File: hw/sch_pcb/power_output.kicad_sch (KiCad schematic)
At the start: 3 parts, among them J2 CONN1_1, J3 CONN1_1, J4 JUMP_4X2

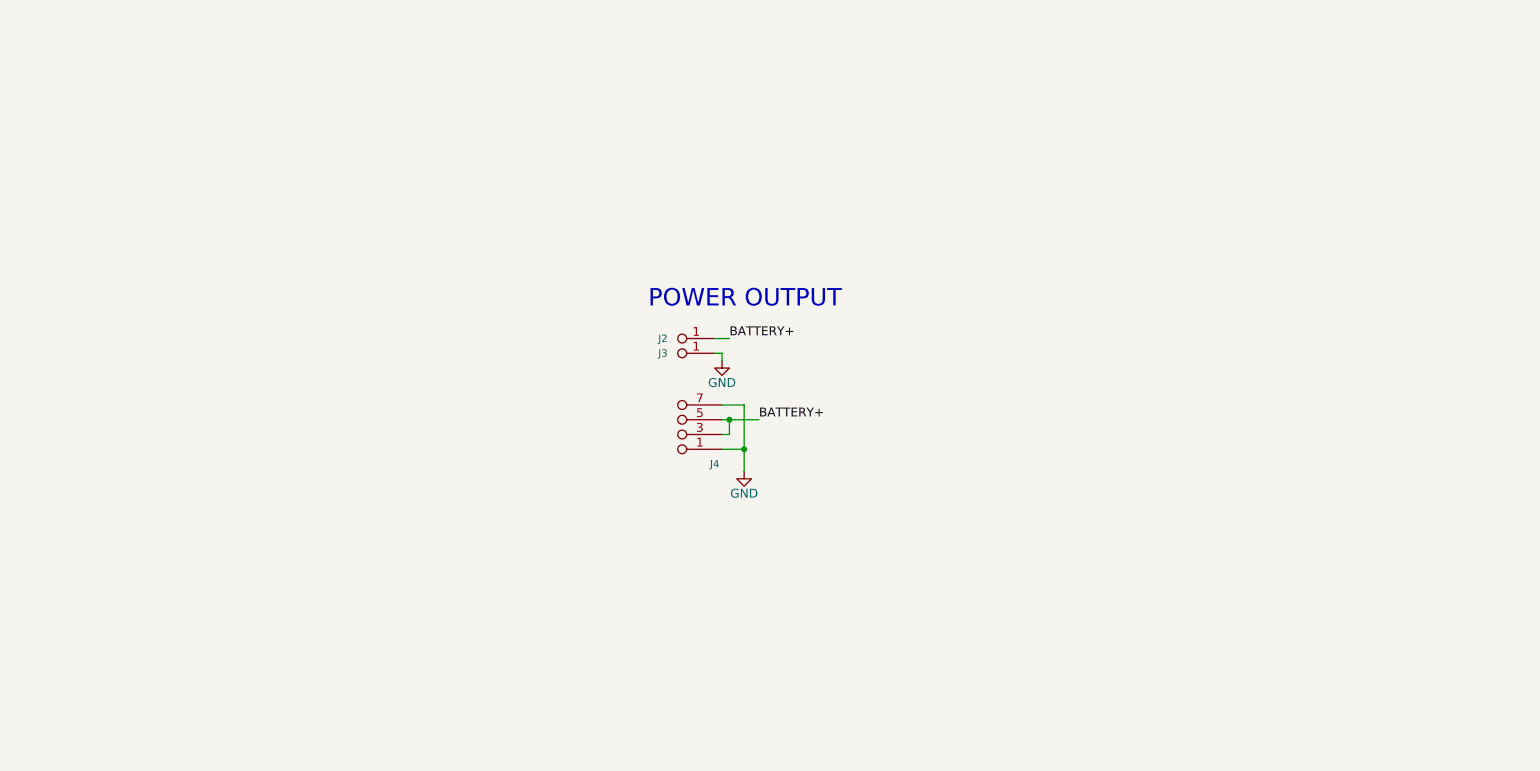
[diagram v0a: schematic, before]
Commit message: Schematics work. PCB layout initial schematics import.
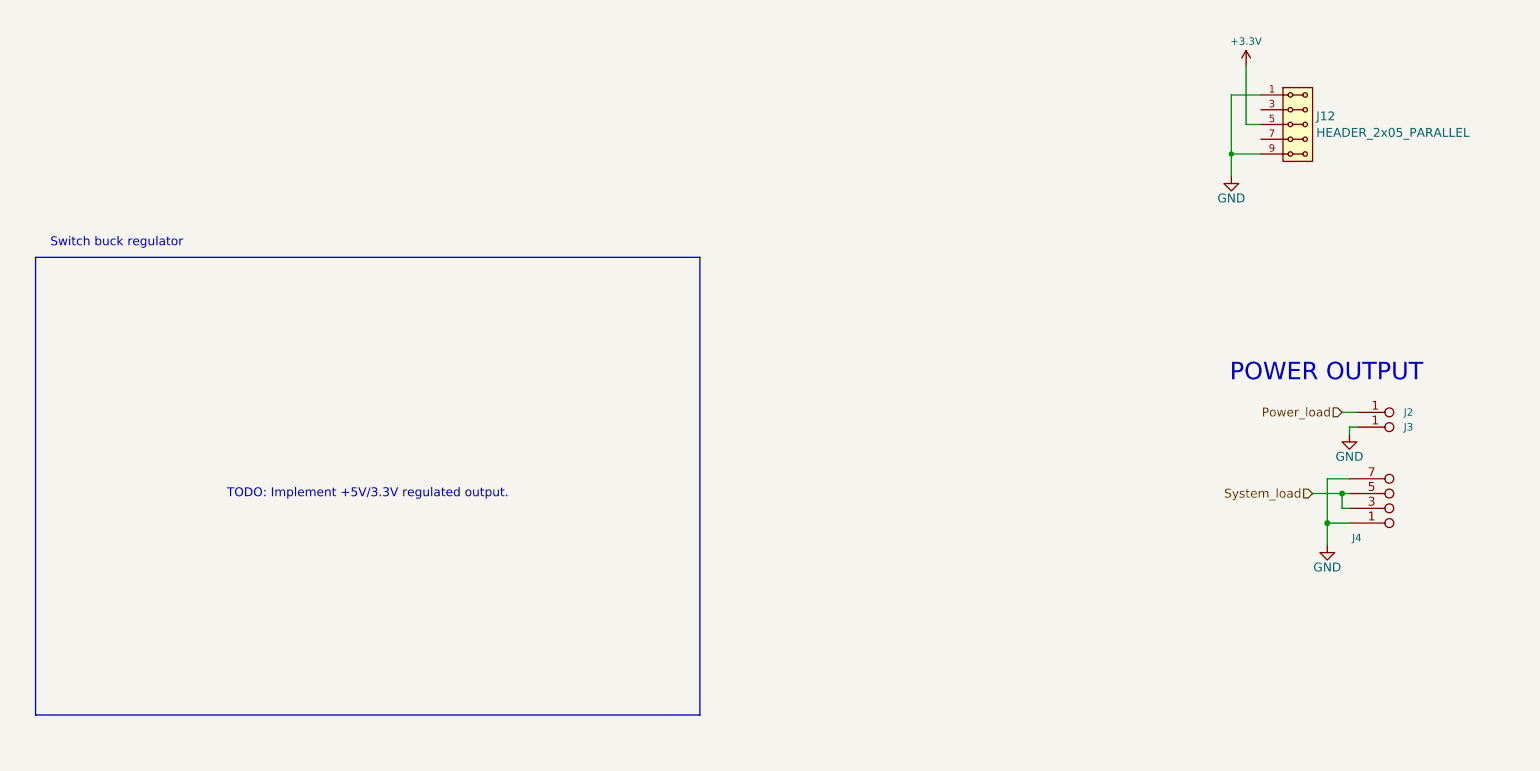
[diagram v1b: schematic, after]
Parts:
- added J12: HEADER_2x05_PARALLEL, Mlab_Pin_Headers:Straight_2x05, symbol MLAB_HEADER:HEADER_2x05_PARALLEL
- J2, J3: footprint Mlab_Con:WAGO256 -> Mlab_CON:WAGO256
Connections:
- net GND: now also J12.1, J12.10, J12.2, J12.9
- net BATTERY+ renamed System_load
- net System_load: no longer J2.1 (P1)
- new net: J12.3, J12.4
- new net: J12.7, J12.8
- new net +3.3V: J12.5, J12.6
- new net Power_load: J2.1 (P1)
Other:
- note added: "Switch buck regulator"
- note added: "TODO: Implement +5V/3.3V regulated output."
- moved on the sheet: J2, J3, J4

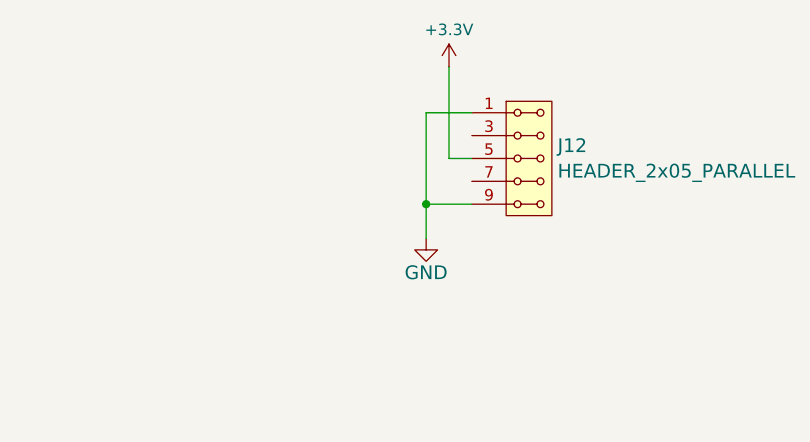
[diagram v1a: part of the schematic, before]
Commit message: Partially routed PCB.
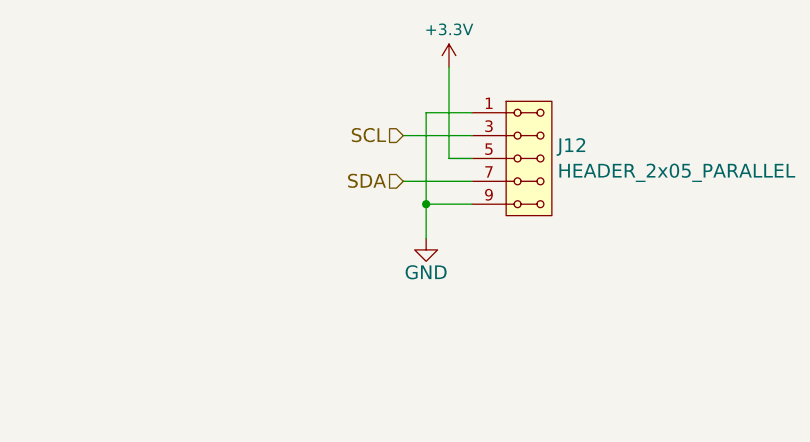
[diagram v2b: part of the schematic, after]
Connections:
- net SCL: now reaches J12.3, J12.4
- net SDA: now reaches J12.7, J12.8
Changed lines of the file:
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@@
+	(wire
+		(pts
+			(xy 233.68 38.1) (xy 241.3 38.1)
+		)
+		(stroke
+			(width 0)
+			(type default)
+		)
+	)
+	(wire
+		(pts
+			(xy 233.68 33.02) (xy 241.3 33.02)
+		)
+		(stroke
+			(width 0)
+			(type default)
+		)
+	)
 	(wire
 		(pts
@@
 		(fields_autoplaced yes)
 		(effects
+			(font
+				(size 1.524 1.524)
+			)
+			(justify right)
+		)
+	)
+	(hierarchical_label "SCL"
+		(shape input)
+		(at 233.68 33.02 180)
+		(fields_autoplaced yes)
+		(effects
+			(font
+				(size 1.524 1.524)
+			)
+			(justify right)
+		)
+	)
+	(hierarchical_label "SDA"
+		(shape input)
+		(at 233.68 38.1 180)
+		(fields_autoplaced yes)
+		(effects

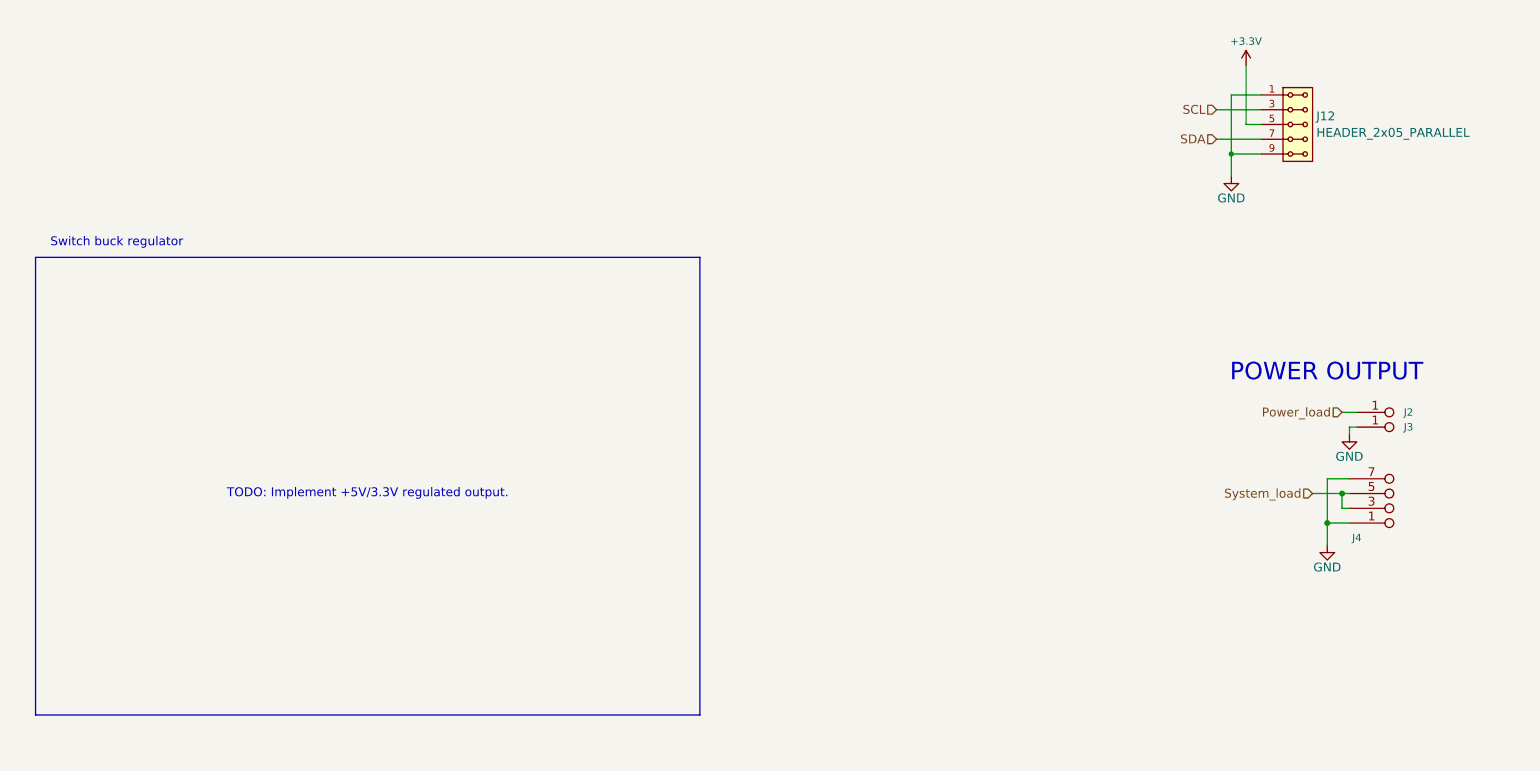
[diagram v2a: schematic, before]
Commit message: Adding output voltage switching regulator.
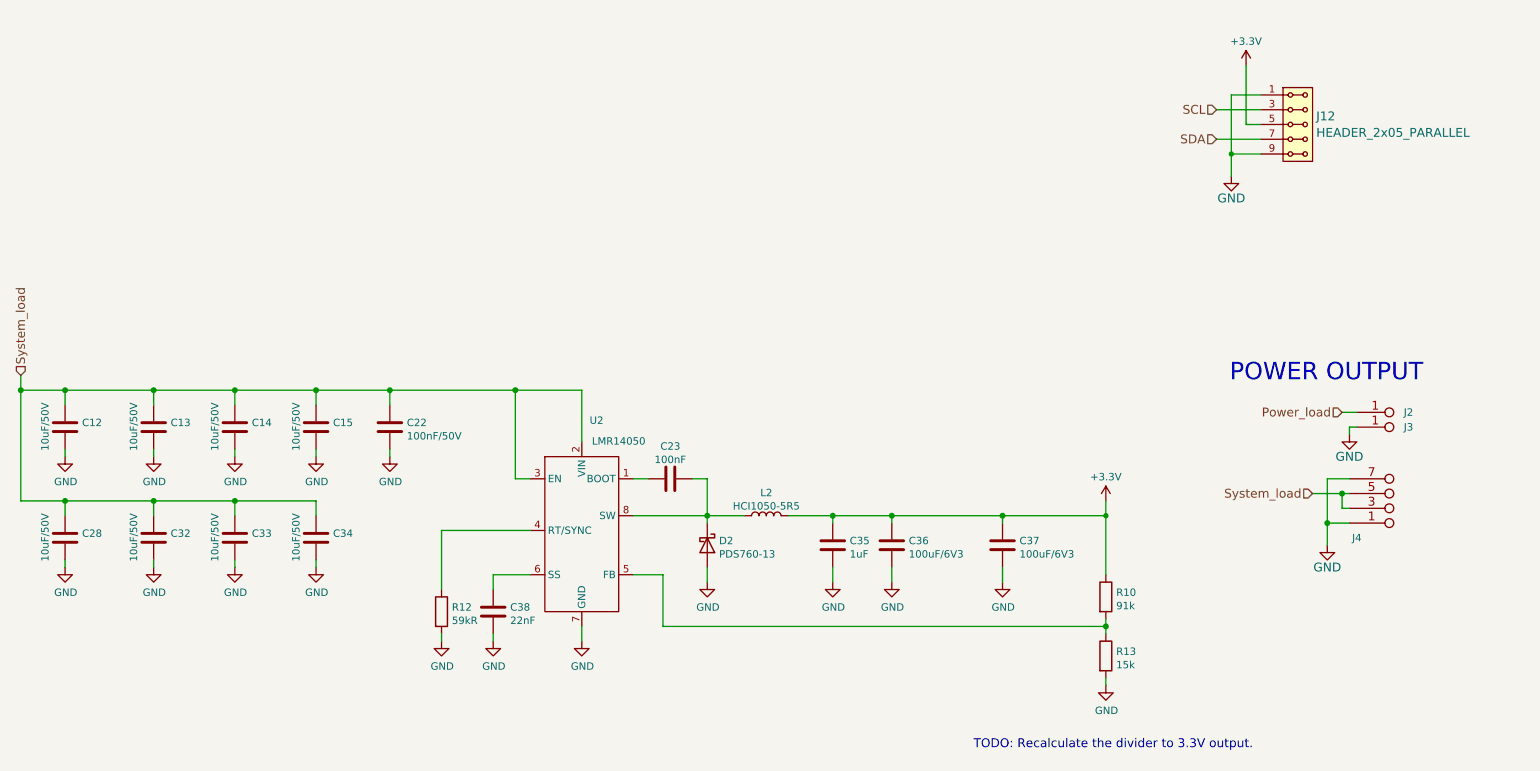
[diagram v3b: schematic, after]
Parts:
- added C12, C13, C14, C15, C28, C32, C33, C34: 10uF/50V, Capacitor_SMD:C_1206_3216Metric, symbol Device:C
- added C22: 100nF/50V, Capacitor_SMD:C_0805_2012Metric, symbol Device:C
- added C23: 100nF, Capacitor_SMD:C_0805_2012Metric, symbol Device:C
- added C35: 1uF, Capacitor_SMD:C_0805_2012Metric, symbol Device:C
- added C36, C37: 100uF/6V3, Capacitor_SMD:C_1206_3216Metric, symbol Device:C
- added C38: 22nF, Capacitor_SMD:C_0805_2012Metric, symbol Device:C
- added D2: PDS760-13, Diode_SMD:D_PowerDI-5, symbol Device:D_Schottky
- added L2: HCI1050-5R5, Inductor_SMD:L_Wuerth_HCI-1050, symbol Device:L
- added R10: 91k, Resistor_SMD:R_0805_2012Metric, symbol Device:R
- added R12: 59kR, Resistor_SMD:R_0805_2012Metric, symbol Device:R
- added R13: 15k, Resistor_SMD:R_0805_2012Metric, symbol Device:R
- added U2: LMR14050, Package_SO:SOIC-8-1EP_3.9x4.9mm_P1.27mm_EP2.41x3.3mm_ThermalVias, symbol MLAB_IO:LMR14050
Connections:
- net +3.3V: now also C35.1, C36.1, C37.1, L2.2, R10.1
- net GND: now also C12.2, C13.2, C14.2, C15.2, C22.2, C28.2, C32.2, C33.2, C34.2, C35.2, C36.2, C37.2, C38.2, D2.2 (A), R12.2, R13.2, U2.7 (GND), U2.9 (GND)
- net System_load: now also C12.1, C13.1, C14.1, C15.1, C22.1, C28.1, C32.1, C33.1, C34.1, U2.2 (VIN), U2.3 (EN)
- new net: C23.1, U2.1 (BOOT)
- new net: C23.2, D2.1 (K), L2.1, U2.8 (SW)
- new net: C38.1, U2.6 (SS)
- new net: R10.2, R13.1, U2.5 (FB)
- new net: R12.1, U2.4 (RT/SYNC)
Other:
- note added: "TODO: Recalculate the divider to 3.3V output."
- note removed: "Switch buck regulator"
- note removed: "TODO: Implement +5V/3.3V regulated output."

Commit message: Minimizing output regulator components count.
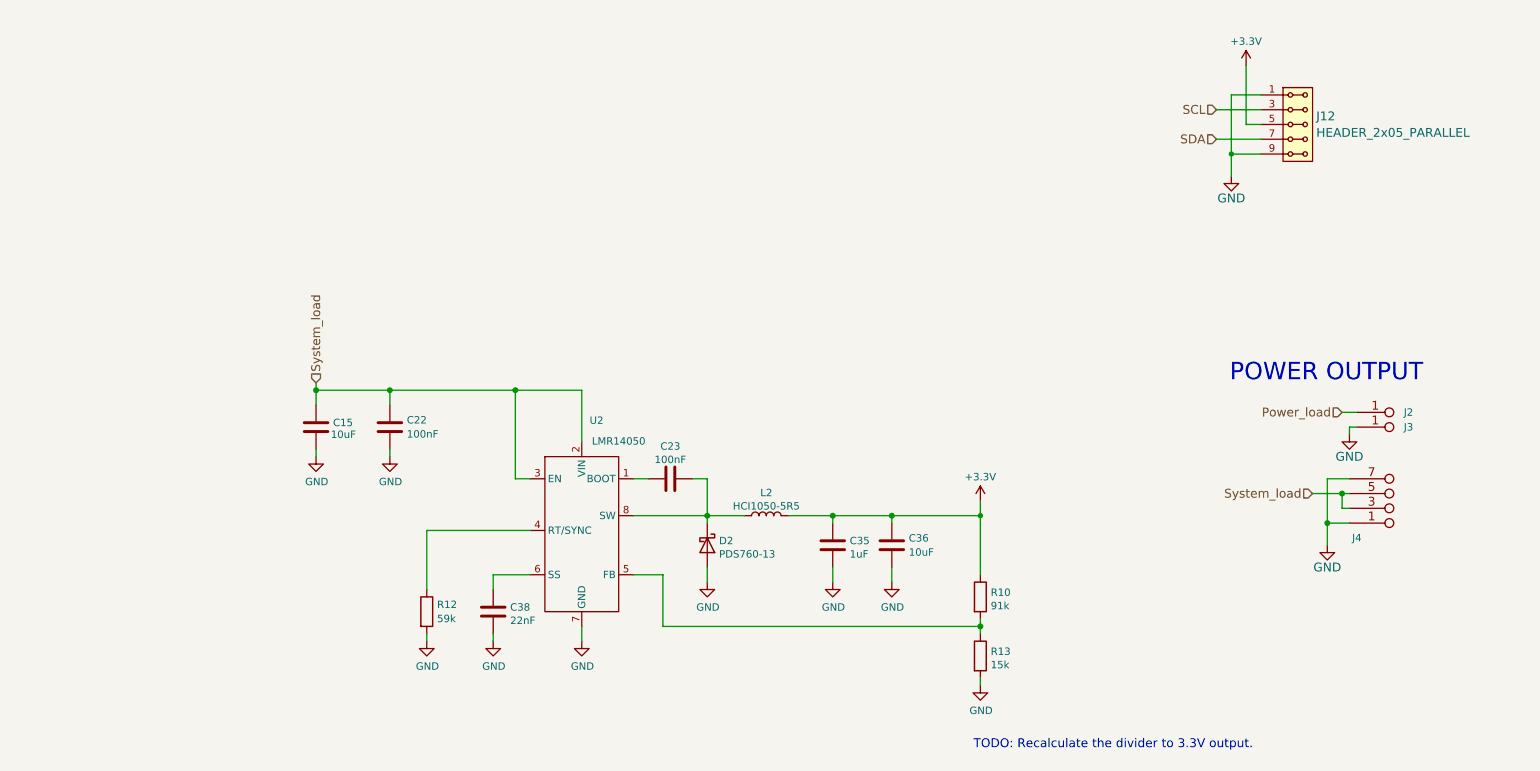
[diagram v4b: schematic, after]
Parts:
- removed C12, C13, C14, C28, C32, C33, C34: 10uF/50V, Capacitor_SMD:C_1206_3216Metric, symbol Device:C
- removed C37: 100uF/6V3, Capacitor_SMD:C_1206_3216Metric, symbol Device:C
- C15: value 10uF/50V -> 10uF
- C22: value 100nF/50V -> 100nF
- C36: value 100uF/6V3 -> 10uF; footprint Capacitor_SMD:C_1206_3216Metric -> Capacitor_SMD:C_0805_2012Metric
- R12: value 59kR -> 59k
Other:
- moved on the sheet: R10, R12, R13

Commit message: update power-output schematic
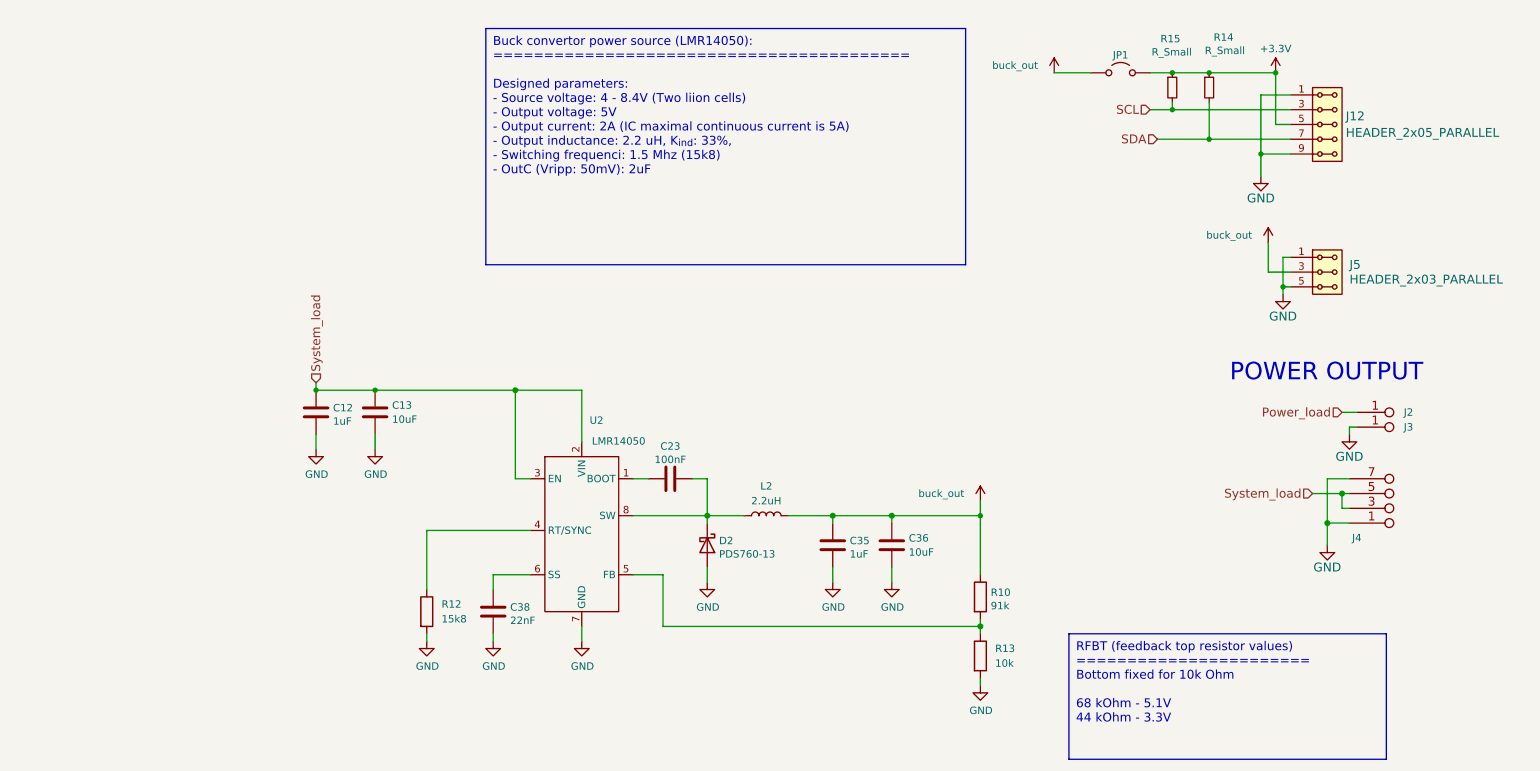
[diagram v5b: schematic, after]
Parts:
- removed C15: 10uF, Capacitor_SMD:C_1206_3216Metric, symbol Device:C
- removed C22: 100nF, Capacitor_SMD:C_0805_2012Metric, symbol Device:C
- added C12: 1uF, Capacitor_SMD:C_0805_2012Metric, symbol Device:C
- added C13: 10uF, Capacitor_SMD:C_0805_2012Metric, symbol Device:C
- added J5: HEADER_2x03_PARALLEL, symbol MLAB_HEADER:HEADER_2x03_PARALLEL
- added JP1: Jumper_2_Open, symbol Jumper:Jumper_2_Open
- added R14, R15: R_Small, symbol Device:R_Small
- L2: value HCI1050-5R5 -> 2.2uH
- R12: value 59k -> 15k8
- R13: value 15k -> 10k; UST_ID 5c70984712875079b91f8b6a -> (none)
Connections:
- net +3.3V: now also JP1.2 (B), R14.1, R15.1; no longer C35.1, C36.1, L2.2, R10.1
- net GND: now also C12.2, C13.2, J5.1, J5.2, J5.5, J5.6
- net SCL: now also R15.2
- net SDA: now also R14.2
- net System_load: now also C12.1, C13.1
- new net buck_out: C35.1, C36.1, J5.3, J5.4, JP1.1 (A), L2.2, R10.1
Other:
- note removed: "TODO: Recalculate the divider to 3.3V output."
- moved on the sheet: J12
